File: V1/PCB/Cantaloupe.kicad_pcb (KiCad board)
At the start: 2 copper layers, 143.9 x 118.7 mm, 87 parts, among them J2 OLED, J3 Link, J5 Trackball, SW1 MX, SW10 MX, SW11 MX, SW12 MX, SW13 MX, SW14 MX, SW15 MX, SW16 MX, SW17 MX, SW18 MX, SW19 MX, SW2 MX, SW20 MX, SW21 MX, SW22 MX, SW23 MX, SW24 MX, SW25 MX, SW26 MX, SW27 MX, SW28 MX, SW29 MX, SW3 MX, SW30 MX, SW31 Encoder, SW32 MX, SW4 MX, SW5 MX, SW6 MX, SW7 MX, SW8 MX, SW9 MX, U1 ProMicro, U3 SRV05-4

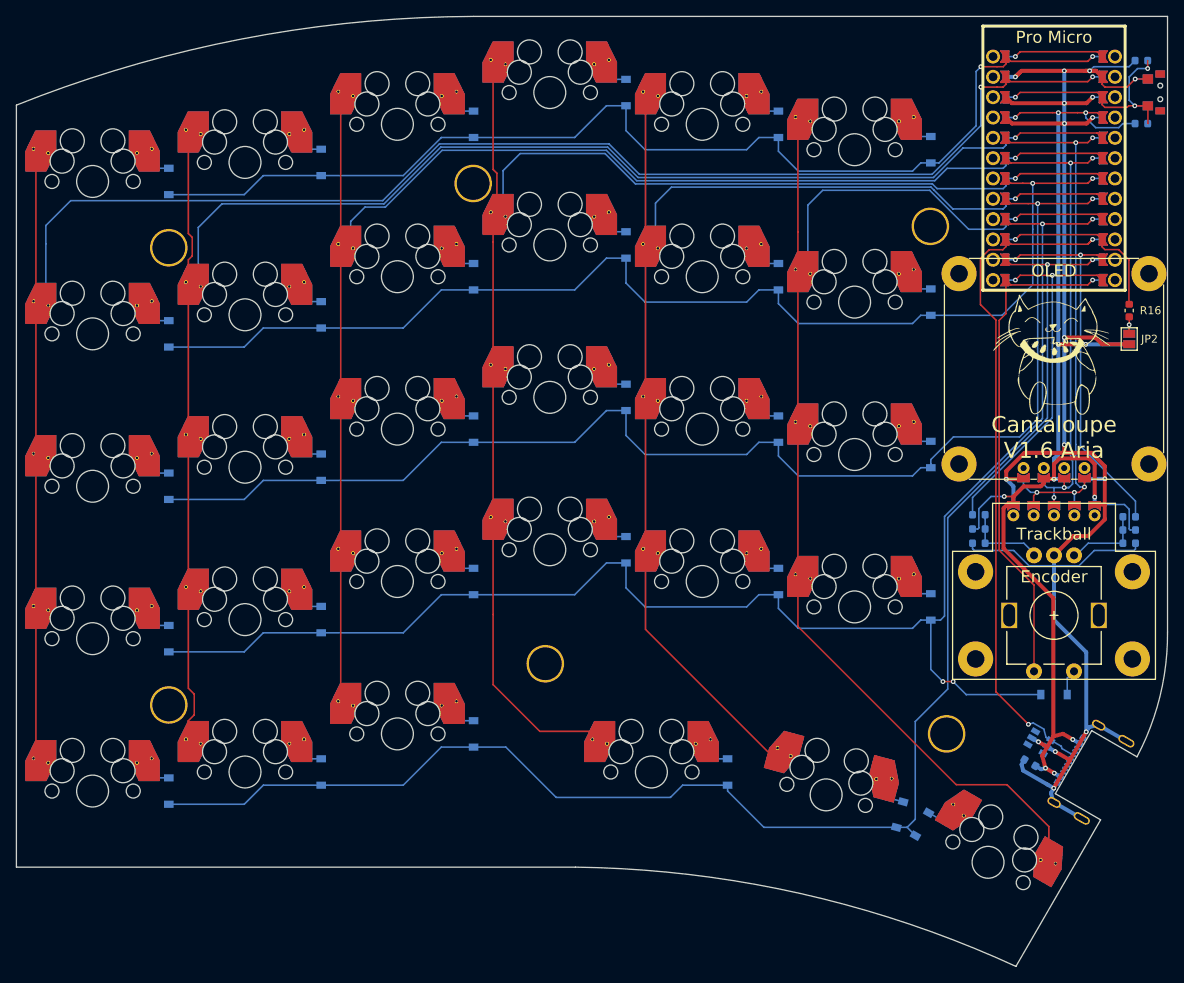
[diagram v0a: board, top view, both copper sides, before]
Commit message: Removed PCB mounting holes. Slightly changed position of reset switch.
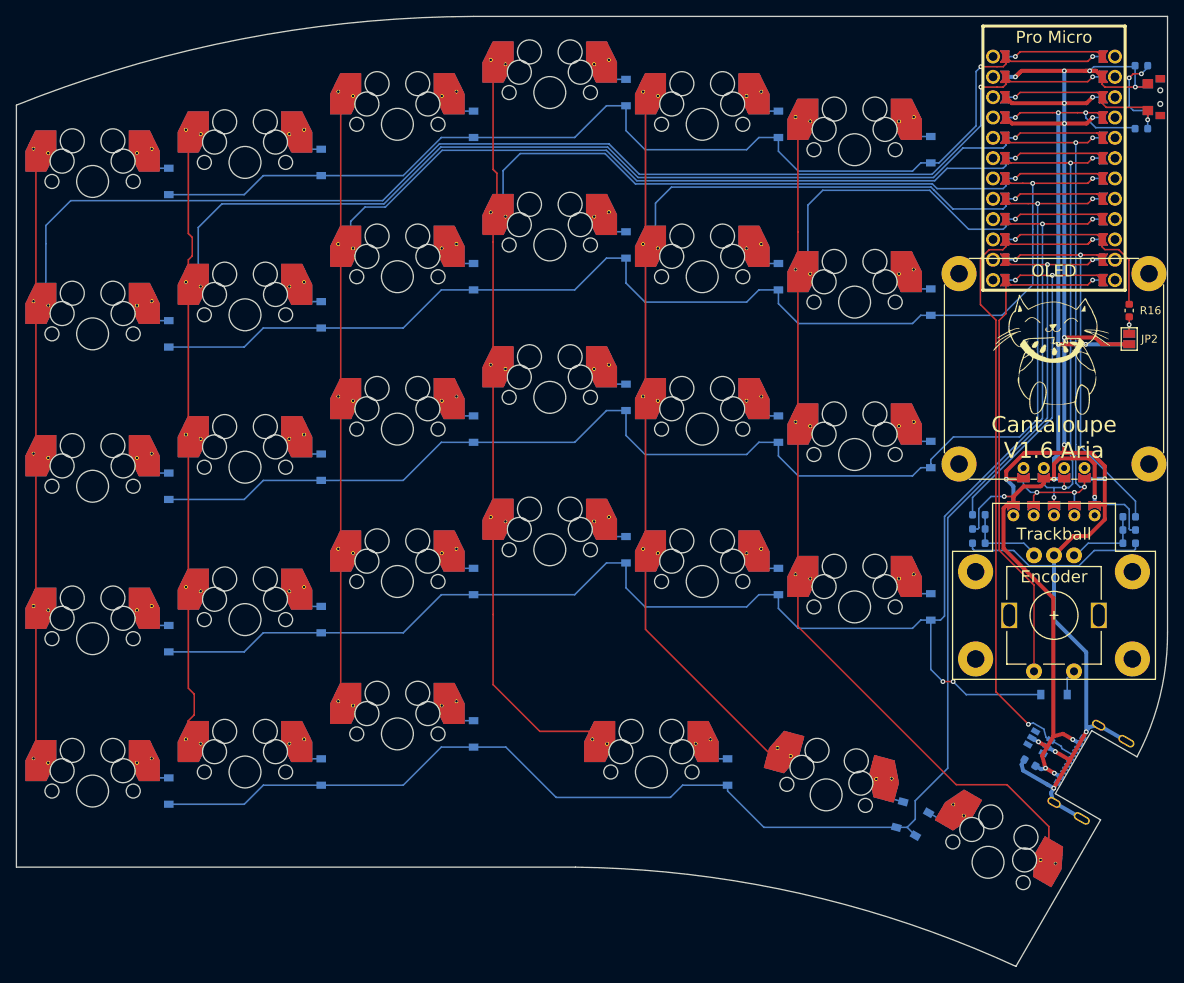
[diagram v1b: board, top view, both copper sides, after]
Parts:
- removed H1, H2, H3, H4, H5, H6: Hole, Ariamelon:HOLE_M2_TH
- U3: value SRV05-4 -> SRV0504
- moved C4 0.64 mm to (154.0, 19.8)
- moved R9 0.63 mm to (154.0, 27.7)
- moved SW32 0.59 mm to (156.3, 23.7)
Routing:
- net GND: track 232.8 -> 235.2 mm
- net RST: track 30.9 -> 32.0 mm, vias 3 -> 4
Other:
- rule pad_to_mask_clearance: 0.051 -> 0
